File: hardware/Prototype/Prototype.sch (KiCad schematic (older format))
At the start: 3 parts

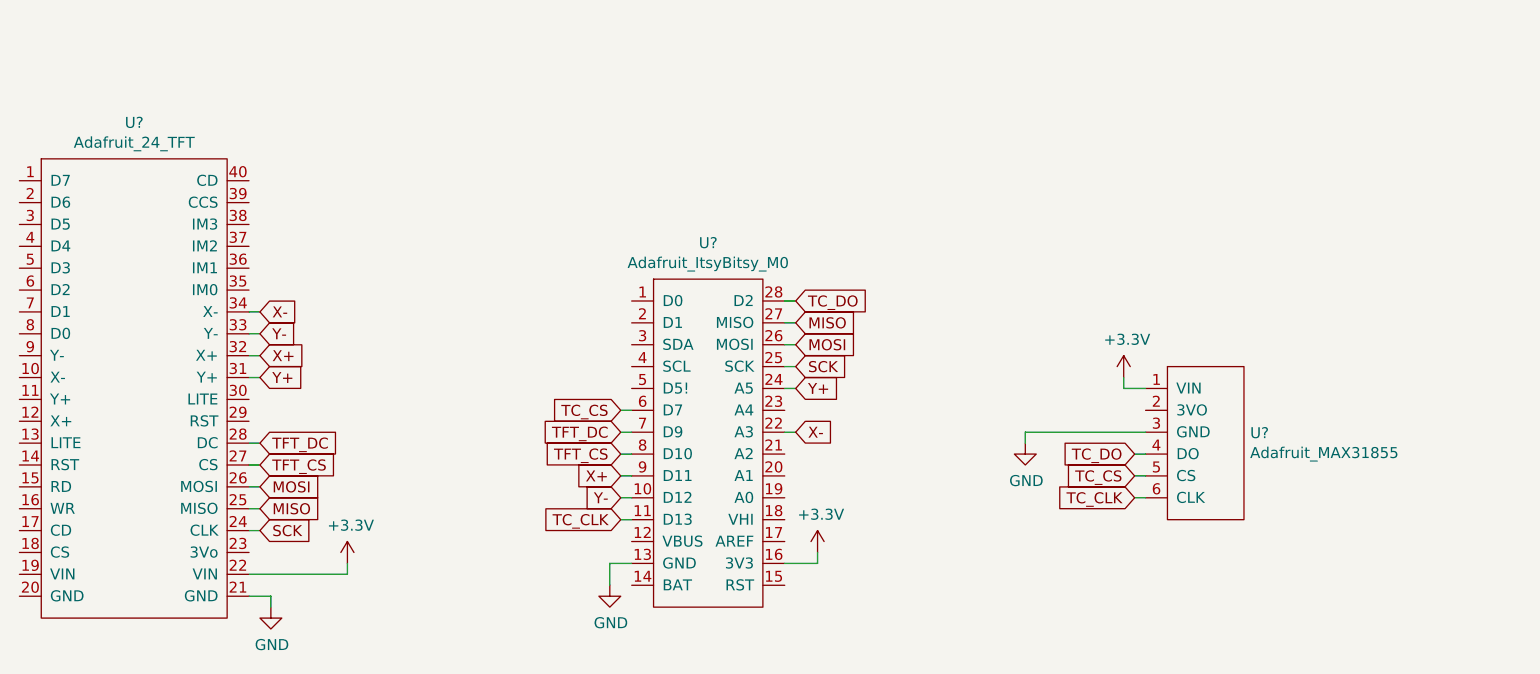
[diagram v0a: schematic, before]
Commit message: Create Prototype Board Layout (#18)
* Add TFT footprint

* Add ItsyBitsy M0 footprint

* Create Thermocouple footprint

* Create prototype board layout
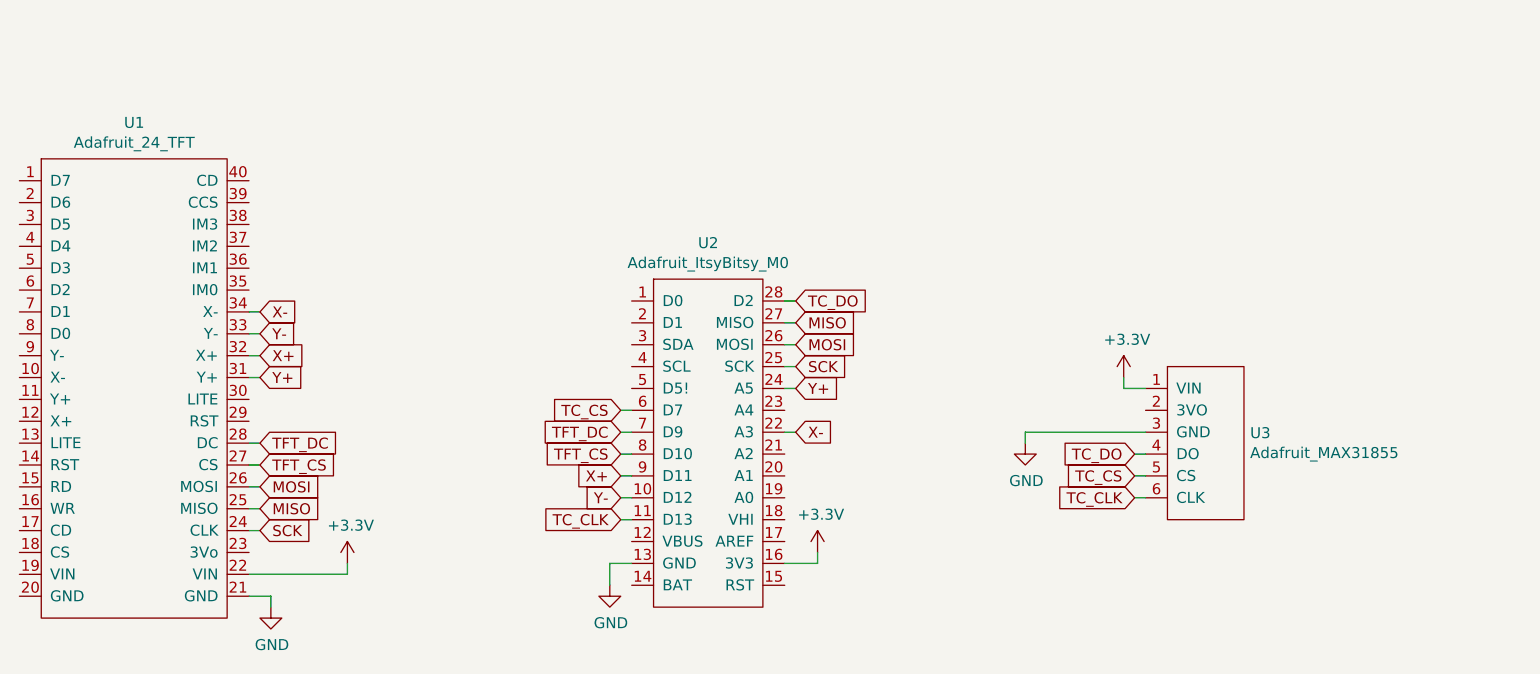
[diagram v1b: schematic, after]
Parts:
- U1: renamed from U?; footprint (none) -> Modules:Adafruit_24_TFT
- U2: renamed from U?; footprint (none) -> Modules:Adafruit_ItsyBitsy_M0
- U3: renamed from U?; footprint (none) -> Modules:Adafruit_MAX31855
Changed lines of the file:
@@
 $EndDescr
 $Comp
-L Modules:Adafruit_24_TFT U?
+L Modules:Adafruit_24_TFT U1
 U 1 1 63260F31
 P 3350 2650
-F 0 "U?" H 3325 2715 50  0000 C CNN
+F 0 "U1" H 3325 2715 50  0000 C CNN
 F 1 "Adafruit_24_TFT" H 3325 2624 50  0000 C CNN
-F 2 "" H 3350 2600 50  0001 C CNN
+F 2 "Modules:Adafruit_24_TFT" H 3350 2600 50  0001 C CNN
 F 3 "" H 3350 2600 50  0001 C CNN
 	1    3350 2650
@@
 $EndComp
 $Comp
-L Modules:Adafruit_ItsyBitsy_M0 U?
+L Modules:Adafruit_ItsyBitsy_M0 U2
 U 1 1 63261DFE
 P 5950 3300
-F 0 "U?" H 5950 3465 50  0000 C CNN
+F 0 "U2" H 5950 3465 50  0000 C CNN
 F 1 "Adafruit_ItsyBitsy_M0" H 5950 3374 50  0000 C CNN
-F 2 "" H 5950 3350 50  0001 C CNN
+F 2 "Modules:Adafruit_ItsyBitsy_M0" H 5950 3350 50  0001 C CNN
 F 3 "" H 5950 3350 50  0001 C CNN
 	1    5950 3300
@@
 $EndComp
 $Comp
-L Modules:Adafruit_MAX31855 U?
+L Modules:Adafruit_MAX31855 U3
 U 1 1 63262A86
 P 8050 3700
-F 0 "U?" H 8428 3396 50  0000 L CNN
+F 0 "U3" H 8428 3396 50  0000 L CNN
 F 1 "Adafruit_MAX31855" H 8428 3305 50  0000 L CNN
-F 2 "" H 8050 3750 50  0001 C CNN
+F 2 "Modules:Adafruit_MAX31855" H 8050 3750 50  0001 C CNN
 F 3 "" H 8050 3750 50  0001 C CNN
 	1    8050 3700
@@
 $EndComp
 $Comp
-L power:+3.3V #PWR?
+L power:+3.3V #PWR02
 U 1 1 6326403D
 P 4300 4600
-F 0 "#PWR?" H 4300 4450 50  0001 C CNN
+F 0 "#PWR02" H 4300 4450 50  0001 C CNN
 F 1 "+3.3V" H 4315 4773 50  0000 C CNN
 F 2 "" H 4300 4600 50  0001 C CNN
@@
 $EndComp
 $Comp
-L power:GND #PWR?
+L power:GND #PWR01
 U 1 1 63264721
 P 3950 4800
-F 0 "#PWR?" H 3950 4550 50  0001 C CNN
+F 0 "#PWR01" H 3950 4550 50  0001 C CNN
 F 1 "GND" H 3955 4627 50  0000 C CNN
 F 2 "" H 3950 4800 50  0001 C CNN
@@
 	3850 4650 4300 4650
 $Comp
-L power:+3.3V #PWR?
+L power:+3.3V #PWR04
 U 1 1 63266DB3
 P 6450 4550
-F 0 "#PWR?" H 6450 4400 50  0001 C CNN
+F 0 "#PWR04" H 6450 4400 50  0001 C CNN
 F 1 "+3.3V" H 6465 4723 50  0000 C CNN
 F 2 "" H 6450 4550 50  0001 C CNN
@@
 $EndComp
 $Comp
-L power:GND #PWR?
+L power:GND #PWR03
 U 1 1 6326720F
 P 5500 4700
-F 0 "#PWR?" H 5500 4450 50  0001 C CNN
+F 0 "#PWR03" H 5500 4450 50  0001 C CNN
 F 1 "GND" H 5505 4527 50  0000 C CNN
 F 2 "" H 5500 4700 50  0001 C CNN
@@
 	6450 4600 6450 4550
 $Comp
-L power:+3.3V #PWR?
+L power:+3.3V #PWR06
 U 1 1 632681A5
 P 7850 3750
-F 0 "#PWR?" H 7850 3600 50  0001 C CNN
+F 0 "#PWR06" H 7850 3600 50  0001 C CNN
 F 1 "+3.3V" H 7865 3923 50  0000 C CNN
 F 2 "" H 7850 3750 50  0001 C CNN
@@
 $EndComp
 $Comp
-L power:GND #PWR?
+L power:GND #PWR05
 U 1 1 63268929
 P 7400 4050
-F 0 "#PWR?" H 7400 3800 50  0001 C CNN
+F 0 "#PWR05" H 7400 3800 50  0001 C CNN
 F 1 "GND" H 7405 3877 50  0000 C CNN
 F 2 "" H 7400 4050 50  0001 C CNN

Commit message: Add SSR connector to controller board
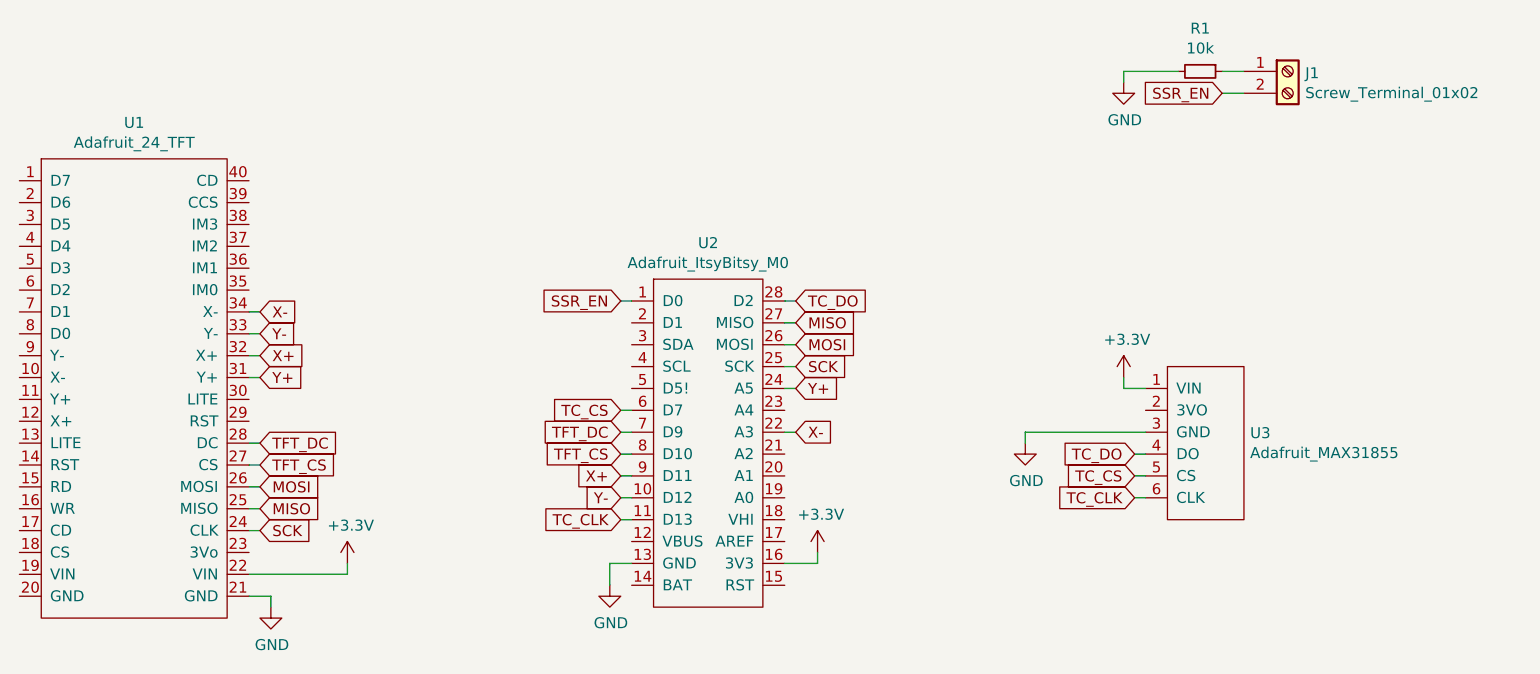
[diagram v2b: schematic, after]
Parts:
- added J1: Screw_Terminal_01x02, TerminalBlock:TerminalBlock_Altech_AK300-2_P5.00mm, symbol Connector:Screw_Terminal_01x02
- added R1: 10k, Resistor_THT:R_Axial_DIN0411_L9.9mm_D3.6mm_P15.24mm_Horizontal, symbol Device:R_Small
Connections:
- net GND: now also R1.2
- net SSR_EN: now reaches U2.1 (D0)
- net SSR_EN: now also J1.2 (Pin_2)
- new net: J1.1 (Pin_1), R1.1
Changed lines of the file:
@@
 Wire Wire Line
 	3900 3450 3850 3450
+$Comp
+L Connector:Screw_Terminal_01x02 J1
+U 1 1 63311BC9
+P 8600 2350
+F 0 "J1" H 8680 2342 50  0000 L CNN
+F 1 "Screw_Terminal_01x02" H 8680 2251 50  0000 L CNN
+F 2 "TerminalBlock:TerminalBlock_Altech_AK300-2_P5.00mm" H 8600 2350 50  0001 C CNN
+F 3 "~" H 8600 2350 50  0001 C CNN
+	1    8600 2350
+	1    0    0    -1
+$EndComp
+Text GLabel 8300 2450 0    50   Input ~ 0
+SSR_EN
+Text GLabel 5550 3400 0    50   Input ~ 0
+SSR_EN
+$Comp
+L Device:R_Small R1
+U 1 1 63314173
+P 8200 2350
+F 0 "R1" V 8004 2350 50  0000 C CNN
+F 1 "10k" V 8095 2350 50  0000 C CNN
+F 2 "Resistor_THT:R_Axial_DIN0411_L9.9mm_D3.6mm_P15.24mm_Horizontal" H 8200 2350 50  0001 C CNN
+F 3 "~" H 8200 2350 50  0001 C CNN
+	1    8200 2350
+	0    1    1    0
+$EndComp
+$Comp
+L power:GND #PWR0101
+U 1 1 63314A7E
+P 7850 2400
+F 0 "#PWR0101" H 7850 2150 50  0001 C CNN
+F 1 "GND" H 7855 2227 50  0000 C CNN
+F 2 "" H 7850 2400 50  0001 C CNN
+F 3 "" H 7850 2400 50  0001 C CNN
+	1    7850 2400
+	1    0    0    -1
+$EndComp
+Wire Wire Line
+	8300 2450 8400 2450
+Wire Wire Line
+	8400 2350 8300 2350
+Wire Wire Line
+	8100 2350 7850 2350
+Wire Wire Line
+	7850 2350 7850 2400
+Wire Wire Line
+	5550 3400 5600 3400
 $EndSCHEMATC
